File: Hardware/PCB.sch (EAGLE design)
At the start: 12 parts, among them IC1 7805T, U1 328P

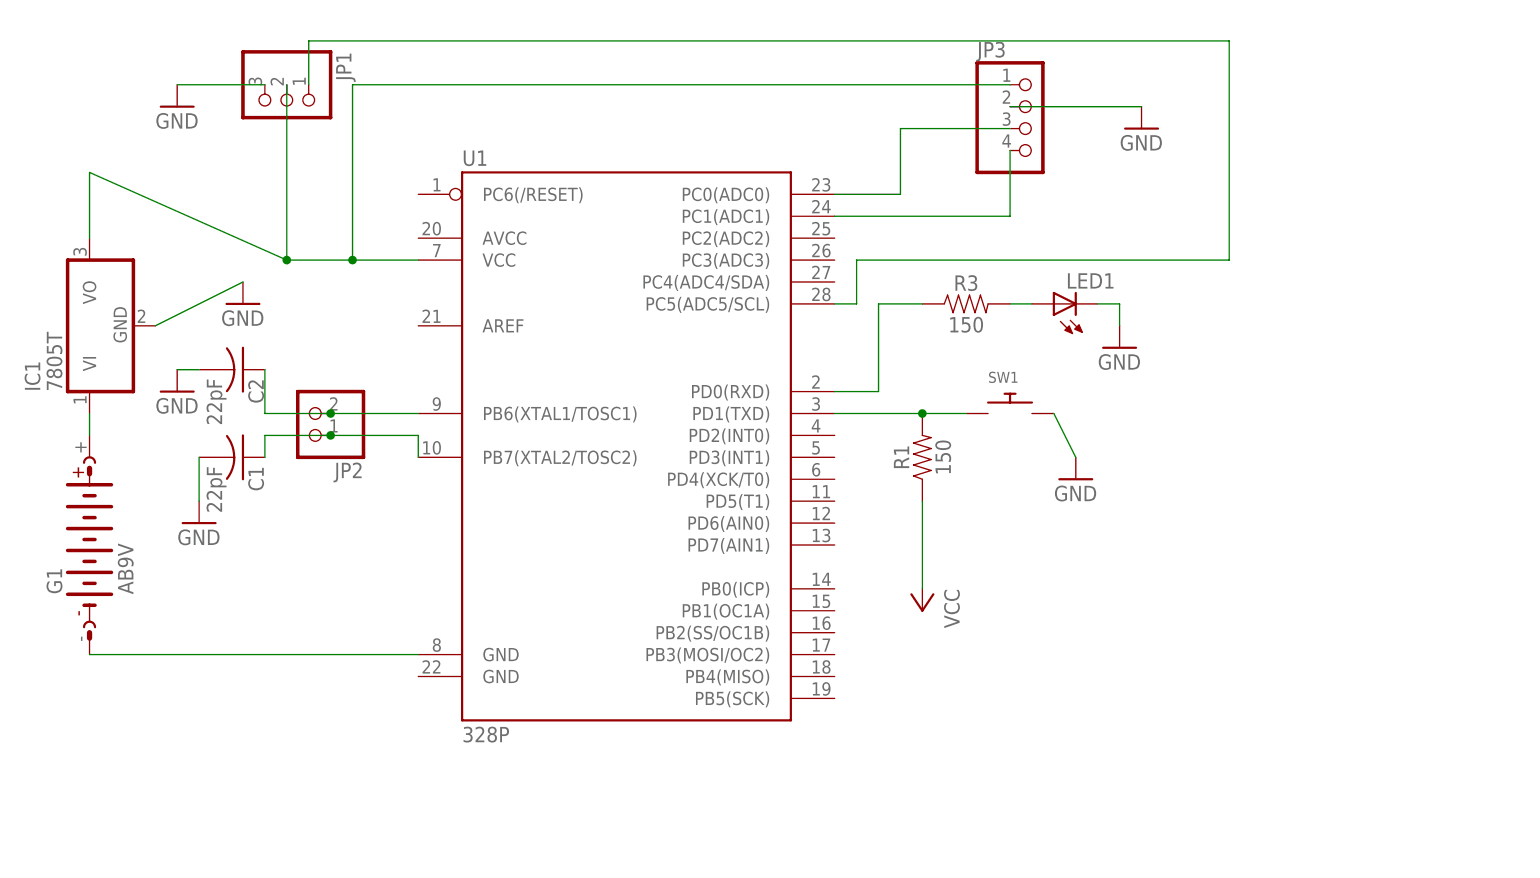
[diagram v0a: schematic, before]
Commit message: Add Final PCB design and remove first PCB iteration
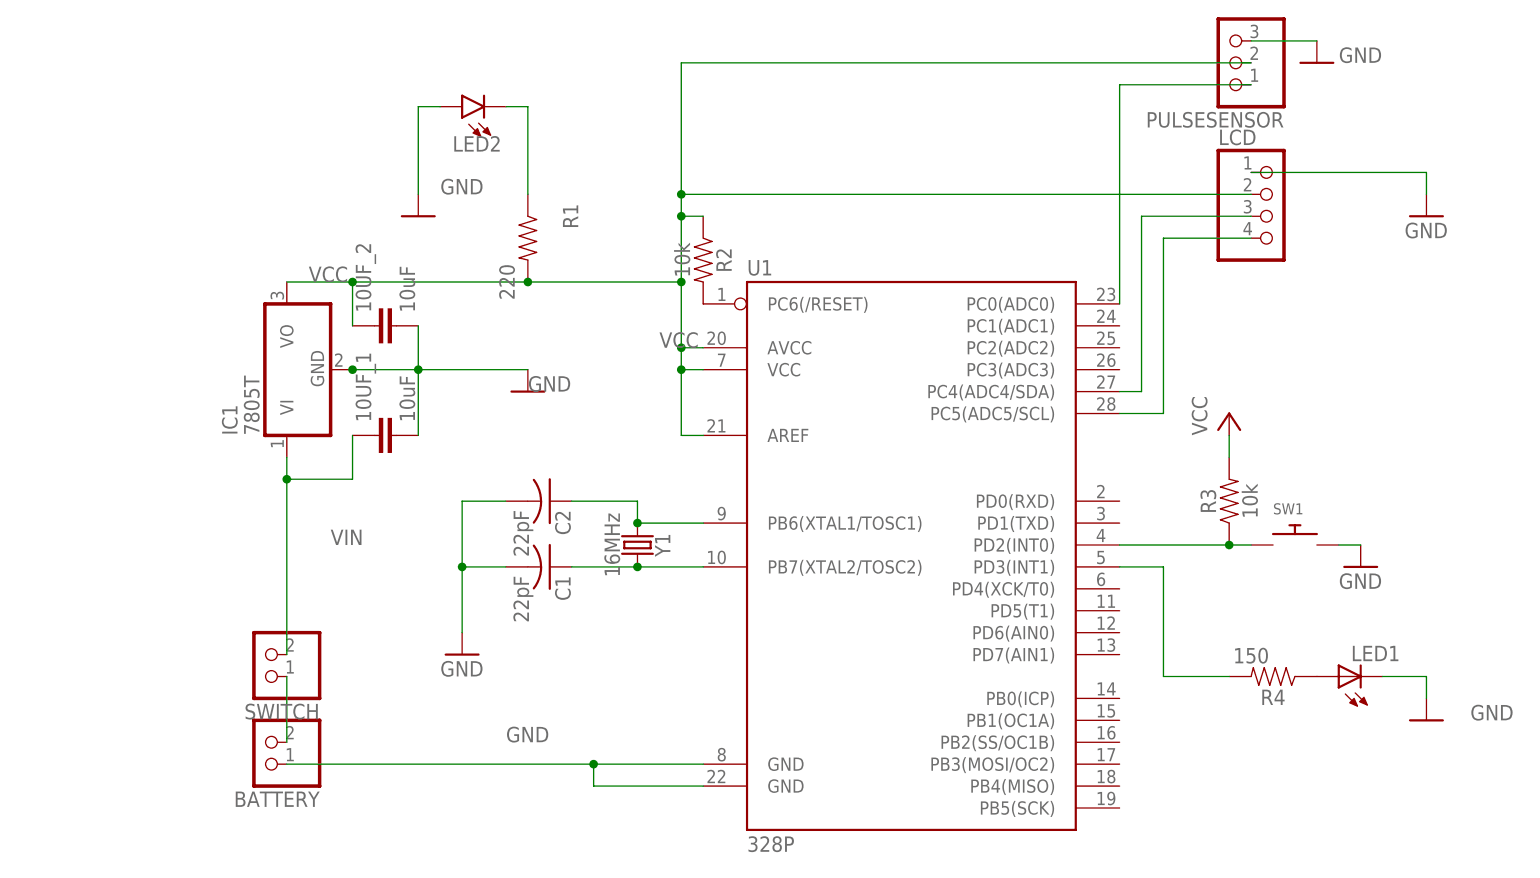
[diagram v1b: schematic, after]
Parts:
- removed G1: AB9V, battery:AB9V
- removed JP1: (no value), adafruit:PINHD-1X3
- removed JP2: (no value), pinhead:PINHD-1X2
- removed JP3: (no value), pinhead:PINHD-1X4
- added 10UF_1, 10UF_2: 10uF, SparkFun-Capacitors:22PF-PTH-2.54MM-200V-5%
- added BATTERY, SWITCH: (no value), pinhead:PINHD-1X2
- added LCD: (no value), pinhead:PINHD-1X4
- added LED2: (no value), SparkFun-LED:LED3MM
- added PULSESENSOR: (no value), adafruit:PINHD-1X3
- added R2: 10k, SparkFun-Resistors:10KOHM-HORIZ-1/4W-5%
- added R4: 150, SparkFun-Resistors:10KOHM-HORIZ-1/4W-5%
- added Y1: 16MHz, SparkFun-Clocks:CRYSTAL-16MHZPTH-HC49US
- R1: value 150 -> 220; device SparkFun-Resistors:150OHM-0603-1/10W-1% -> SparkFun-Resistors:10KOHM-HORIZ-1/4W-5%
- R3: value 150 -> 10k; device SparkFun-Resistors:150OHM-0603-1/10W-1% -> SparkFun-Resistors:10KOHM-HORIZ-1/4W-5%
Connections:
- removed net N$10: R1.2, SW1.P$1, U1.PD1(TXD)
- removed net N$12: JP1.1, U1.PC5(ADC5/SCL)
- removed net N$2: JP3.4, U1.PC1(ADC1)
- removed net N$5: IC1.VO, JP1.2, JP3.1, U1.VCC
- removed net N$6: LED1.A, R3.2
- removed net N$7: R3.1, U1.PD0(RXD)
- removed net N$8: C2.1, JP2.2, U1.PB6(XTAL1/TOSC1)
- removed net N$9: C1.1, JP2.1, U1.PB7(XTAL2/TOSC2)
- new net PC0/ADC0: PULSESENSOR.1, U1.PC0(ADC0)
- new net PD2: R4.2, U1.PD3(INT1)
- new net PD3: R3.1, SW1.P$1, U1.PD2(INT0)
- new net RESET: R2.2, U1.PC6(/RESET)
- new net SCL: LCD.4, U1.PC5(ADC5/SCL)
- new net SDA: LCD.3, U1.PC4(ADC4/SDA)
- new net VIN: 10UF_1.1, IC1.VI, SWITCH.2
- new net XTAL1: C2.1, U1.PB6(XTAL1/TOSC1), Y1.1
- new net XTAL2: C1.1, U1.PB7(XTAL2/TOSC2), Y1.2
- net GND: now also 10UF_1.2, 10UF_2.2, BATTERY.1, LCD.1, LED2.A, PULSESENSOR.3, U1.GND@1, U1.GND@2; no longer JP1.3, JP3.2
- net N$1: now also BATTERY.2, SWITCH.1; no longer JP3.3, U1.PC0(ADC0)
- net N$3: now also LED1.A, R4.1; no longer G1.+, IC1.VI
- net N$4: now also LED2.C, R1.1; no longer G1.-, U1.GND@1
- net VCC: now also 10UF_2.1, IC1.VO, LCD.2, PULSESENSOR.2, R1.2, R2.1, R3.2, U1.AREF, U1.AVCC, U1.VCC; no longer R1.1
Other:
- moved on the sheet: C1, C2, IC1, LED1, R1, R3, SW1, U1
